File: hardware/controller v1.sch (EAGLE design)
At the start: 11 parts, among them IC2 L293DD"

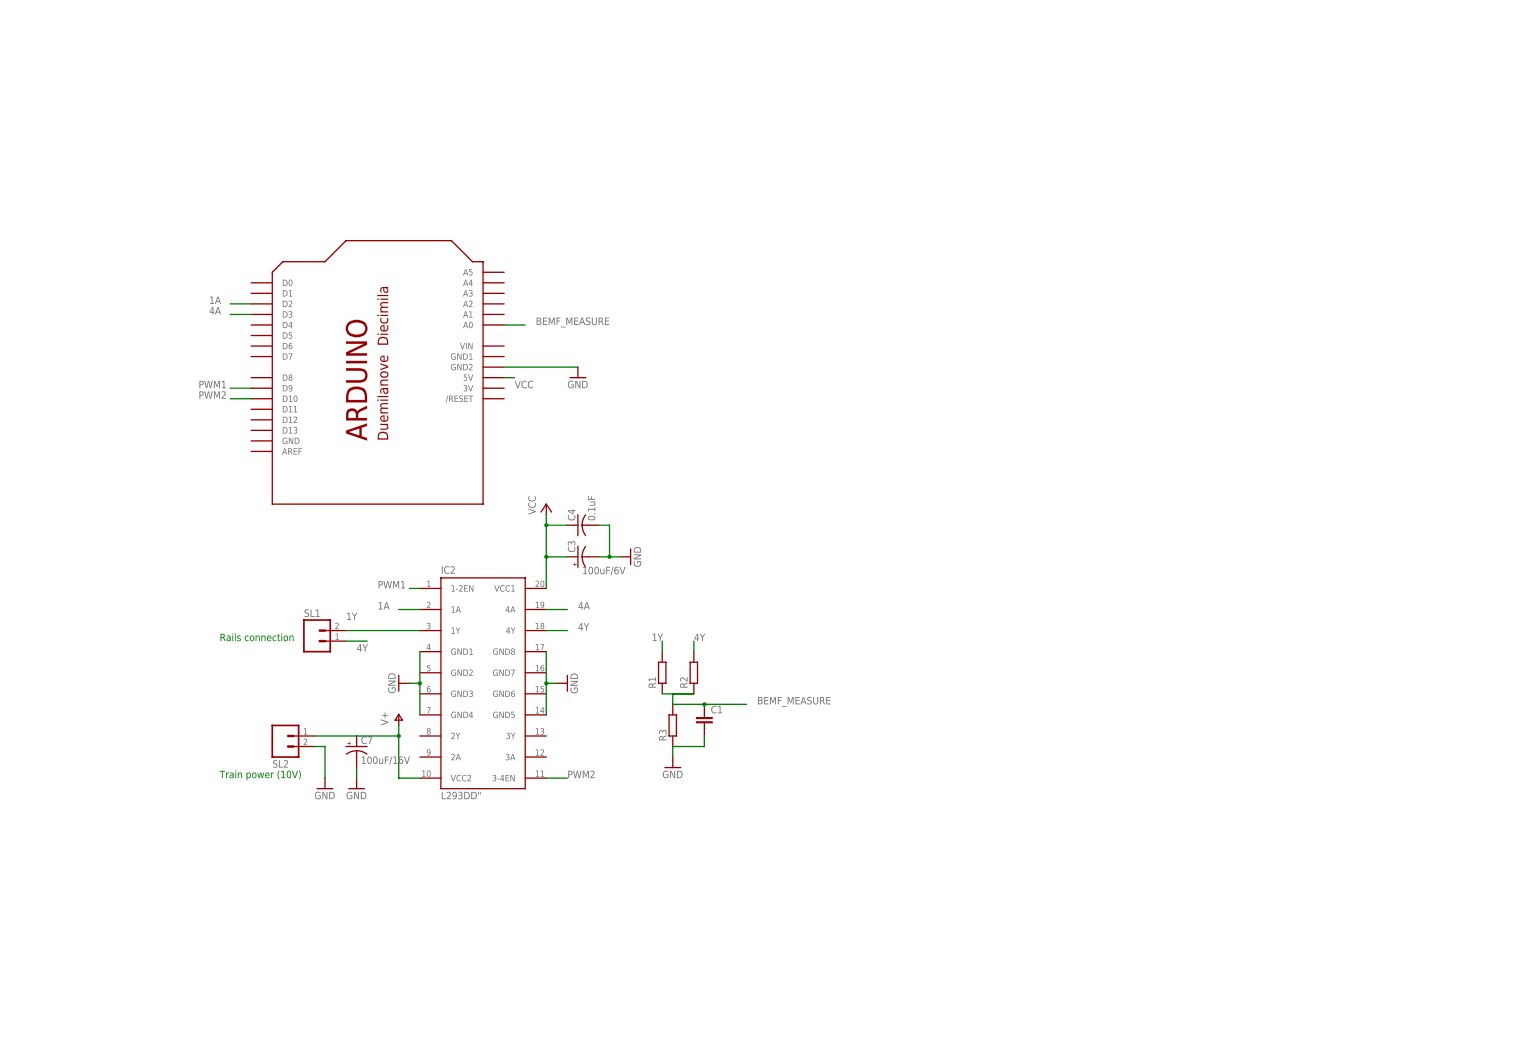
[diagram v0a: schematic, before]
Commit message: Update on hardware schematics for Arduino shield
Final version will probably be a Beaglebone shield rather than Arduino,
but Arduino is so simple for testing...
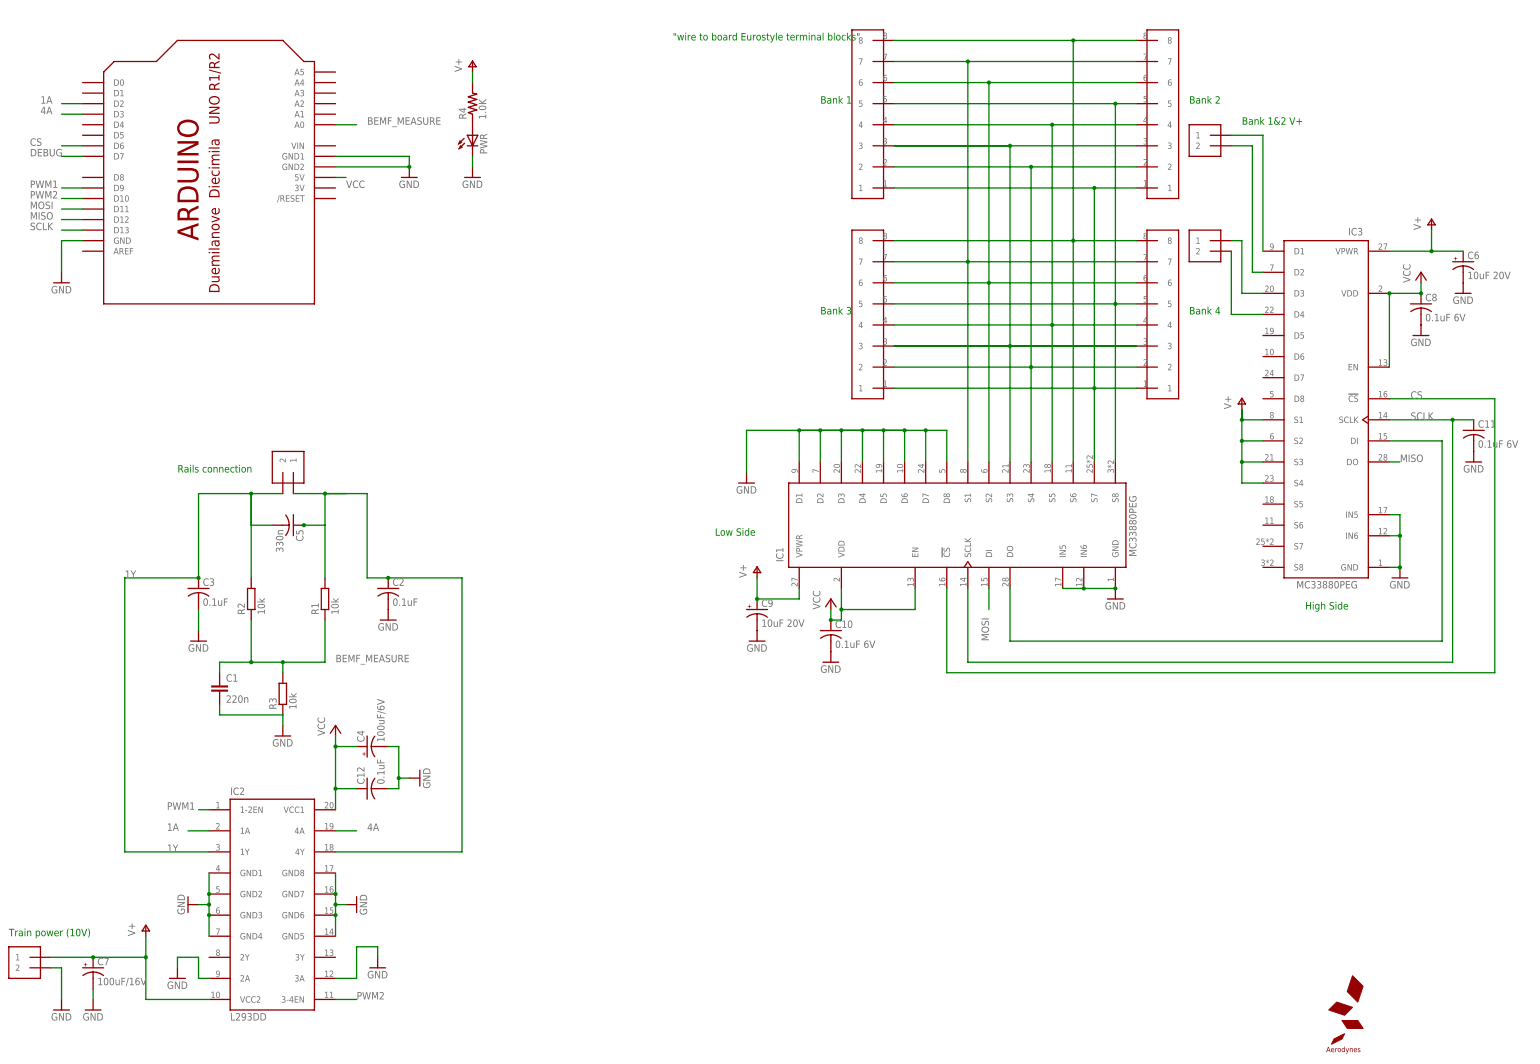
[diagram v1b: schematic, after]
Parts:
- added BANK12, BANK34: 1X2-3.5MM, adafruit:1X2-3.5MM
- added C10, C11, C8: 0.1uF 6V, rcl-ez:C-US025-025X050
- added C12, C2: 0.1uF, rcl-ez:C-US025-025X050
- added C5: 330n, adafruit:C-US050-025X075
- added C6, C9: 10uF 20V, rcl:CPOL-USE2,5-6E
- added CON1, CON2, CON3, CON4: 1X08-CONN3.5MM, aerodynes:1X08-CONN3.5MM
- added IC1, IC3: MC33880PEG, aerodynes:MC33880PEG
- added PWR: (no value), minimidi:LED3MM
- added R4: 1.0K, rcl-ez:R-US_M0805
- added U$2: LOGO-AERODYNESSMALL, aerodynes:LOGO-AERODYNESSMALL
- C1: value (none) -> 220n
- C3: value 100uF/6V -> 0.1uF; device rcl-ez:CPOL-USE2.5-5 -> rcl-ez:C-US025-025X050
- C4: value 0.1uF -> 100uF/6V; device rcl-ez:C-US025-025X050 -> adafruit:CPOL-USE2.5-5
- IC2: value L293DD" -> L293DD
- R1, R2, R3: value (none) -> 10k
- SL1, SL2: value (none) -> 1X2-3.5MM; device con-amp-quick:M02 -> adafruit:1X2-3.5MM
- U$1: value ARDUINOUNO -> ARDUINO; device adafruit:ARDUINOUNO -> aerodynes:ARDUINO
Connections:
- new net CS: IC1.!CS, IC3.!CS, U$1.D6
- new net DEBUG: U$1.D7
- new net MISO: IC3.DO, U$1.D12
- new net MOSI: IC1.DI, U$1.D11
- new net N$1: BANK12.2, IC3.D2
- new net N$11: CON1.1, CON2.1, CON3.1, CON4.1, IC1.S7
- new net N$12: CON1.8, CON2.8, CON3.8, CON4.8, IC1.S6
- new net N$13: IC1.DO, IC3.DI
- new net N$14: CON1.7, CON2.7, CON3.7, CON4.7, IC1.S1
- new net N$15: CON1.2, CON2.2, CON3.2, CON4.2, IC1.S4
- new net N$16: CON1.6, CON2.6, CON3.6, CON4.6, IC1.S2
- new net N$2: BANK12.1, IC3.D1
- new net N$3: BANK34.1, IC3.D3
- new net N$35: PWR.A, R4.1
- new net N$4: BANK34.2, IC3.D4
- new net N$7: CON1.3, CON2.3, CON3.3, CON4.3, IC1.S3
- new net N$8: CON1.4, CON2.4, CON3.4, CON4.4, IC1.S5
- new net N$9: CON1.5, CON2.5, CON3.5, CON4.5, IC1.S8
- new net SCLK: C11.1, IC1.SCLK, IC3.SCLK, U$1.D13
- net 1Y: now also C3.1, C5.2, R2.2; no longer R1.2
- net 4Y: now also C2.1, C5.1, R1.2; no longer R2.2
- net GND: now also C10.2, C11.2, C12.2, C2.2, C3.2, C4.-, C6.-, C8.2, C9.-, IC1.D1, IC1.D2, IC1.D3, IC1.D4, IC1.D5, IC1.D6, IC1.D7, IC1.D8, IC1.GND, IC1.IN5, IC1.IN6, IC2.2A, IC2.3A, IC2.GND2, IC2.GND3, IC2.GND6, IC2.GND7, IC3.GND, IC3.IN5, IC3.IN6, PWR.C, U$1.GND, U$1.GND1; no longer C3.-, C4.2
- net V+: now also C6.+, C9.+, IC1.VPWR, IC3.S1, IC3.S2, IC3.S3, IC3.S4, IC3.VPWR, R4.2
- net VCC: now also C10.1, C12.1, C4.+, C8.1, IC1.EN, IC1.VDD, IC3.EN, IC3.VDD; no longer C3.+, C4.1
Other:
- note added: ""wire to board Eurostyle terminal blocks""
- note added: "Bank 1"
- note added: "Bank 1&2 V+"
- note added: "Bank 2"
- note added: "Bank 3"
- note added: "Bank 4"
- note added: "High Side"
- note added: "Low Side"
- moved on the sheet: C1, C7, IC2, R1, R2, R3

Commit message: Big bugfix on hardware controller schematics and board.
The 33880 pinout was reversed on my schematics...
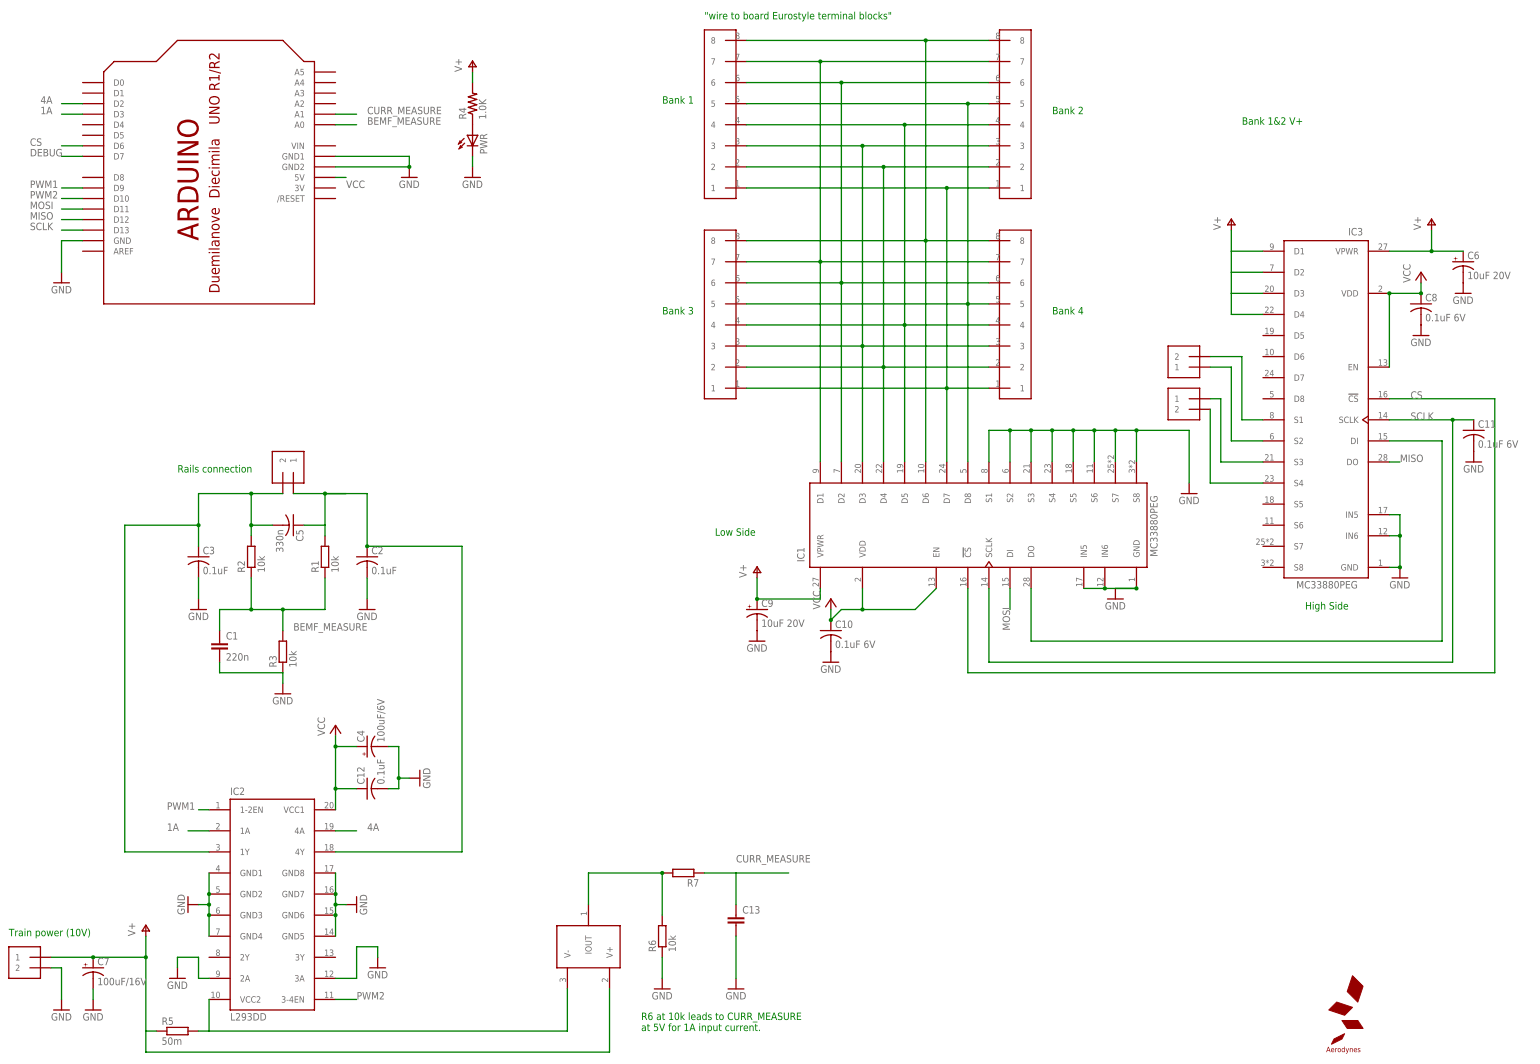
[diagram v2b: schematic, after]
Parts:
- added C13: (no value), resistor:C-EUC0805K
- added R5: 50m, resistor:R-EU_M1206
- added R6: 10k, resistor:R-EU_R0603
- added R7: (no value), resistor:R-EU_R0603
- added U$3: ZXCT1009-F, aerodynes:ZXCT1009-F
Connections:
- new net CURR_MEASURE: C13.1, R7.1, U$1.A1
- new net N$5: IC2.VCC2, R5.2, U$3.V-
- new net N$6: R6.2, R7.2, U$3.IOUT
- net 1A: now also U$1.D3; no longer U$1.D2
- net 4A: now also U$1.D2; no longer U$1.D3
- net GND: now also C13.2, IC1.S1, IC1.S2, IC1.S3, IC1.S4, IC1.S5, IC1.S6, IC1.S7, IC1.S8, R6.1; no longer IC1.D1, IC1.D2, IC1.D3, IC1.D4, IC1.D5, IC1.D6, IC1.D7, IC1.D8
- net N$1: now also BANK34.2, IC3.S4; no longer BANK12.2, IC3.D2
- net N$11: now also IC1.D7; no longer IC1.S7
- net N$12: now also IC1.D6; no longer IC1.S6
- net N$14: now also IC1.D1; no longer IC1.S1
- net N$15: now also IC1.D4; no longer IC1.S4
- net N$16: now also IC1.D2; no longer IC1.S2
- net N$2: now also BANK34.1, IC3.S3; no longer BANK12.1, IC3.D1
- net N$3: now also BANK12.1, IC3.S2; no longer BANK34.1, IC3.D3
- net N$4: now also BANK12.2, IC3.S1; no longer BANK34.2, IC3.D4
- net N$7: now also IC1.D3; no longer IC1.S3
- net N$8: now also IC1.D5; no longer IC1.S5
- net N$9: now also IC1.D8; no longer IC1.S8
- net V+: now also IC3.D1, IC3.D2, IC3.D3, IC3.D4, R5.1, U$3.V+; no longer IC2.VCC2, IC3.S1, IC3.S2, IC3.S3, IC3.S4
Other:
- note added: "R6 at 10k leads to CURR_MEASURE at 5V for 1A input current."
- moved on the sheet: C1, C2, C3, IC1, R1, R2, R3
